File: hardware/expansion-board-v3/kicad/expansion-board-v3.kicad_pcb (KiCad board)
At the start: 6 copper layers, 100 x 62 mm, 178 parts, among them J1 J3_HAT_2x20_SMD排针, J2 U.FL_GNSS_EXT(经尾线转SMA), J4 USB-C_16P, J5 U.FL_978, J6 U.FL_1090_EXT(经尾线转SMA), J7 U.FL_IFA_TEST(π后调试口), J8 U.FL→内置patch, Q2 AO3401A, Q3 AO3401A, Q4 AO3401A, Q5 AO3401A, SW1 RESET短接焊盘, SW2 BOOTSEL短接焊盘, U1 ME6211C33M5, U10 CC1312R1F3RGZR, U11 QPL9547TR7, U12 BGA2817, U14 AD8313ARMZ, U15 TLV3501(TOKMAS), U16 XA17-G4K, U17 XA17-G4K, U2 TPS7A2033PDBVR, U3 TPS7A2033PDBVR, U4 BNO085, U5 BMP388, U6 QMC5883P, U7 ATGM336H-6N-74, U8 RP2040, U9 W25Q128JVSIQ, Y1 12MHz CL=10pF ABM8-272-T3, Y2 48MHz ABM8W-7pF, Y3 32.768kHz FC-135

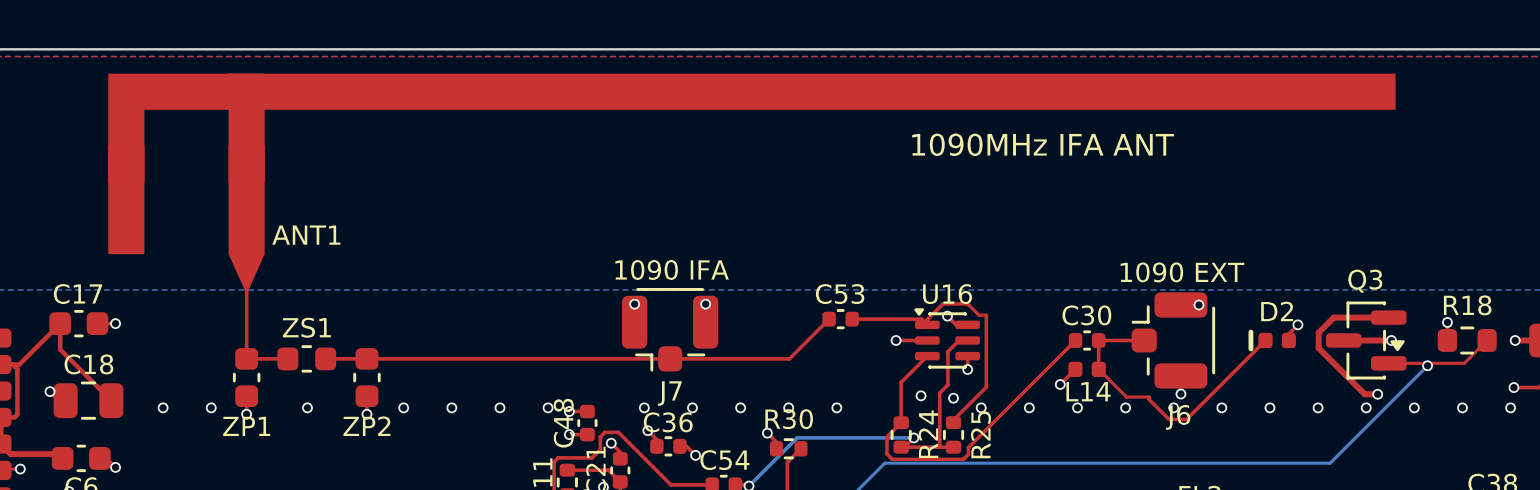
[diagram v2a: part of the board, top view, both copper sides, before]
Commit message: fix(pcb): 补上顶部禁铜带的 3.5mm 断口，换封装后强制重灌覆铜
天线开路端外侧本该全空，实际被 GND 铺铜灌了进去——倒 F 天线电场最强的
一头压着铜。**这正是旧版 IFA 被干扰的同一个病。**

## 根因：禁铜带是三块拼的，只有中间那块跟着天线走

    板级 ANT1090_short_end_keepout   板左沿 → ANT1 禁铜区左沿   坐标写死
    ANT1 封装自带的禁铜区             跟着天线几何走
    板级 ANT1090_open_end_keepout    ANT1 禁铜区右沿 → 板右沿   坐标写死

主臂由 53.5 缩到 50.0mm 后中间那块缩了 3.5mm，两边纹丝不动，带子上开了个
洞（v4 125.422..128.922 / v3 131.722..135.222）。gen_pcb.py 的注释里白纸
黑字写着"改天线位置要一起改"，但**写死的坐标不会提醒任何人**。

参考设计（4.3 原板）那条禁铜带是横跨整块板的矩形。所以判据不是"天线周围
留 2mm"，是**整条带从板左沿到板右沿连续**。

## 为什么整套自动检查都没抓到

    kicad-cli pcb drc --refill-zones   在内存里重填再检查 → 看到"填对的板子"
    kicad-cli pcb export gerbers       导出文件里存着的旧填充

「DRC 0 违例」和「Gerber 是错的」不矛盾，可以同时成立；而 gerber.sh 正是
这个顺序。焊盘落位检查只验"焊盘有没有对应 Flash"，铺铜多一块它不管。
缝里本来就没走线，DRC 更没话说。**只有看整块板才看得见。**

## 改动

- 两个 integrate_ifa_*.py：换 ANT1 后把两侧板级禁铜区贴合到 ANT1 禁铜区的
  **实测包围盒**，断言三块首尾相接铺满整板宽；Save 前 ZONE_FILLER 重灌
- gen_pcb.py：写死坐标改成从 ANT1 封装实测推导，否则整板重建洞会回来
- 新增 test_zone_fill_currency.py（5 项）：
  · 存盘覆铜必须是最新的（读板→记面积→内存重灌→比，通用，不针对天线）
  · 禁铜区内全铜层无铺铜（网格采样，点须严格落在区内）
  · 顶部禁铜带必须贯穿整板宽
  · 两条**坏样本自检**——现造"改了几何没重灌"和"带子断开"的板，
    验证上面的契约确实会红。写完就宣布有效是没有依据的
- test_v4_placement_contract：TP2–TP7 间距由 2.50 收到 2.033mm，
  跟随用户 2026-09-04 的手工重排（合同的既定口径是跟随实际板面）

## 验证

两版 kicad-cli pcb drc（**不加 --refill-zones**，验文件本身）0 违例 0 未连通；
顶部条带逐行与改动前对比完全一致，只剩射频馈线出口那一段；
投板 Gerber 6 层 19788 点采样落铜 0。

过程中我在同一处又犯了一次：用 KEEPOUT_LOCAL[3]（那是脚末端 y）当禁铜区
下沿，比多边形真实下沿少半个线宽，横向的洞刚补上又开了个纵向的。
**取实测边界，不要用公式重算。**
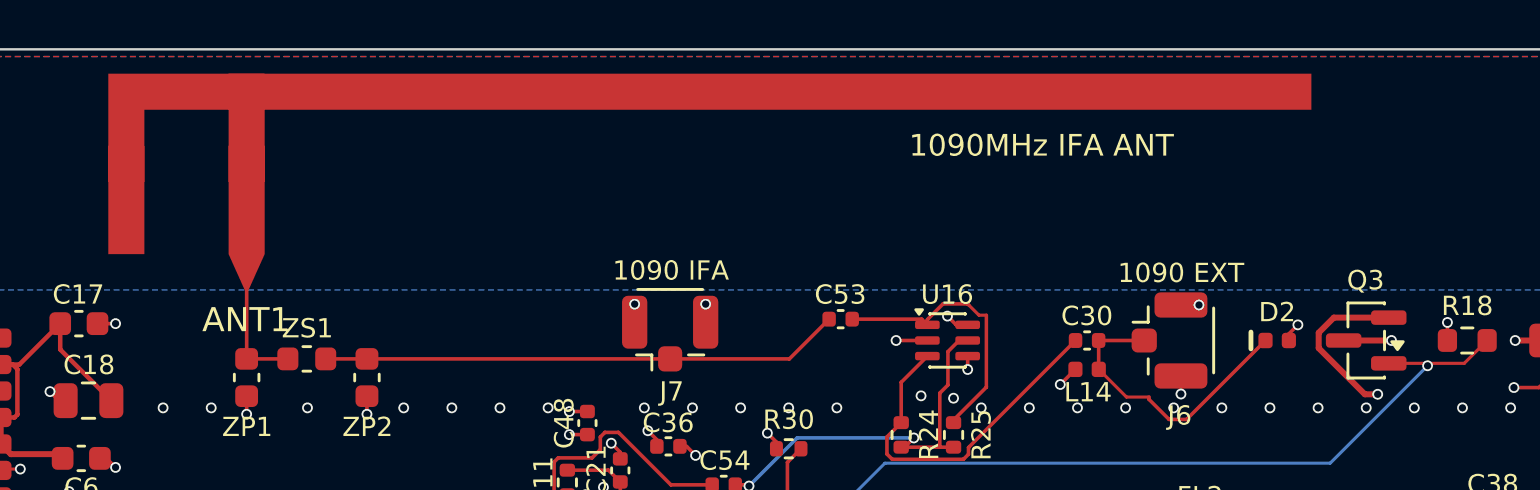
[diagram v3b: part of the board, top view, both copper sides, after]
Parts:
- ANT1: footprint expansion-board-v3:ANT_IFA_1090MHz -> ANT_IFA_1090MHz
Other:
- board text added: "V3.10 2026-09"
- board text removed: "V3.9 2026-09"
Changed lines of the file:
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@@
 		)
 	)
-	(footprint "expansion-board-v3:ANT_IFA_1090MHz"
-		(layer "F.Cu")
-		(at 85.46 57.75)
-		(descr "1090MHz 板载 IFA（完整六层rev2预研冻结画长）。主臂 52.0mm(名义切1.8mm至50.2mm；连续铜箔可按VNA继续切短) / 脚 6.0mm / 两脚中心距 4.988mm / 全段 1.5mm 等宽 / 四周净空 2.0mm。包络 53.5x7.5mm。脚全程在净空内，末端撞入 GND 铺铜。馈电腿铜箔外沿后含1.5mm长 1.5→0.15mm taper（几何rev2）。已 X 镜像使开路端远离 C6 2.4G 天线。")
-		(tags "antenna IFA 1090MHz ADS-B")
-		(property "Reference" "ANT1"
-			(at 2.54 0 0)
-			(layer "F.SilkS")
-			(effects
-				(font
-					(size 0.8 0.8)
-					(thickness 0.15)
-				)
-			)
-		)
-		(property "Value" "IFA_1090"
-			(at 0 5.2 0)
-			(layer "F.Fab")
-			(effects
-				(font
-					(size 1 1)
-					(thickness 0.15)
-				)
-			)
-		)
-		(property "Datasheet" ""
-			(at 0 0 0)
-			(layer "F.Fab")
-			(hide yes)
-			(effects
-				(font
-					(size 1.27 1.27)
-				)
-			)
-		)
-		(property "Description" ""
-			(at 0 0 0)
-			(layer "F.Fab")
-			(hide yes)
-			(effects
-				(font
-					(size 1.27 1.27)
-				)
-			)
-		)
-		(attr smd allow_missing_courtyard)
-		(net_tie_pad_groups "1, 2")
-		(duplicate_pad_numbers_are_jumpers no)
-		(fp_rect
-			(start -5.738 -6.738)
-			(end 47.762 0.762)
-			(stroke
-				(width 0.1)
-				(type default)
-			)
-			(fill no)
-			(layer "F.Fab")
-		)
-		(pad "1" smd custom
-			(at 0.012 -2.988)
-			(size 1.5 1.5)
-			(layers "F.Cu")
-			(net "ANT1090_IFA")
-			(options
-				(clearance outline)
-				(anchor rect)
-			)
-			(primitives
-				(gr_poly
-					(pts
-						(xy -0.75 3.75) (xy 0.75 3.75) (xy 0.75 -3.75) (xy -0.75 -3.75)
-					)
-					(width 0)
-					(fill yes)
-				)
-				(gr_poly
-					(pts
-						(xy -4.25 -3.75) (xy 47.75 -3.75) (xy 47.75 -2.25) (xy -4.25 -2.25)
-					)
-					(width 0)
-					(fill yes)
-				)
-				(gr_poly
-					(pts
-						(xy -0.75 3.75) (xy 0.75 3.75) (xy 0.075 5.25) (xy -0.075 5.25)
-					)
-					(width 0)
-					(fill yes)
-				)
-			)
-		)
-		(pad "2" smd custom
-			(at -4.988 -2.988)
-			(size 1.5 1.5)
-			(layers "F.Cu")
-			(net "GND")
-			(options
-				(clearance outline)
-				(anchor rect)
-			)
-			(primitives
-				(gr_poly
-					(pts
-						(xy -0.75 -3.75) (xy 0.75 -3.75) (xy 0.75 3.75) (xy -0.75 3.75)
-					)
-					(width 0)
-					(fill yes)
-				)
-			)
-		)
-		(zone
-			(layer "F.Cu")
-			(name "ifa_feed_channel")
-			(hatch edge 0.5)
-			(connect_pads
-				(clearance 0)
-			)
-			(min_thickness 0.25)
-			(keepout
-				(tracks allowed)
-				(vias allowed)
-				(pads allowed)
-				(copperpour not_allowed)
-				(footprints allowed)
-			)
-			(placement
-				(enabled no)
-				(sheetname "")
-			)
-			(fill
-				(thermal_gap 0.5)
-				(thermal_bridge_width 0.5)
-				(island_removal_mode 0)
-			)
-			(polygon
-				(pts
-					(xy 84.272 57.762) (xy 86.672 57.762) (xy 86.672 60.012) (xy 84.272 60.012)
-				)
-			)
-		)
-		(zone
-			(layers "F.Cu" "B.Cu" "In1.Cu" "In2.Cu" "In3.Cu" "In4.Cu")
-			(name "ifa_keepout")
-			(hatch edge 0.5)
-			(connect_pads
-				(clearance 0)
-			)
-			(min_thickness 0.25)
-			(keepout
-				(tracks not_allowed)
-				(vias not_allowed)
-				(pads allowed)
-				(copperpour not_allowed)
-				(footprints allowed)
-			)
-			(placement
-				(enabled no)
-				(sheetname "")
-			)
-			(fill
-				(thermal_gap 0.5)
-				(thermal_bridge_width 0.5)
-				(island_removal_mode 0)
-			)
-			(polygon
-				(pts
-					(xy 77.722 50.077) (xy 135.222 50.077) (xy 135.222 58.512) (xy 86.672 58.512) (xy 86.672 57.762)
-					(xy 84.272 57.762) (xy 84.272 58.512) (xy 77.722 58.512)
-				)
-			)
-		)
-		(embedded_fonts no)
-	)
 	(footprint "Connector_Coaxial:U.FL_Hirose_U.FL-R-SMT-1_Vertical"
 		(layer "F.Cu")
@@
 		)
 	)
+	(footprint "ANT_IFA_1090MHz"
+		(layer "F.Cu")
+		(at 85.46 57.75)
+		(descr "1090MHz 板载 IFA（V4.0实板装盒VNA定型）。主臂中心线 48.5mm / 脚 6.0mm / 两脚中心距 4.988mm / 全段 1.5mm 等宽 / 四周净空 2.0mm。包络 50.0x7.5mm。脚全程在净空内，末端撞入 GND 铺铜。馈电腿铜箔外沿后含1.5mm长 1.5→0.15mm taper（几何rev2）。已 X 镜像使开路端远离 C6 2.4G 天线。")
+		(tags "antenna IFA 1090MHz ADS-B")
+		(property "Reference" "ANT1"
+			(at 0 3.5 0)
+			(layer "F.SilkS")
+			(effects
+				(font
+					(size 1 1)
+					(thickness 0.15)
+				)
+			)
+		)
+		(property "Value" "IFA_1090"
+			(at 0 5.2 0)
+			(layer "F.Fab")
+			(effects
+				(font
+					(size 1 1)
+					(thickness 0.15)
+				)
+			)
+		)
+		(property "Datasheet" ""
+			(at 0 0 0)
+			(layer "F.Fab")
+			(hide yes)
+			(effects
+				(font
+					(size 1.27 1.27)
+				)
+			)
+		)
+		(property "Description" ""
+			(at 0 0 0)
+			(layer "F.Fab")
+			(hide yes)
+			(effects
+				(font
+					(size 1.27 1.27)
+				)
+			)
+		)
+		(attr smd allow_missing_courtyard)
+		(net_tie_pad_groups "1, 2")
+		(duplicate_pad_numbers_are_jumpers no)
+		(fp_rect
+			(start -5.738 -6.738)
+			(end 44.262 0.762)
+			(stroke
+				(width 0.1)
+				(type default)
+			)
+			(fill no)
+			(layer "F.Fab")
+		)
+		(pad "1" smd custom
+			(at 0.012 -2.988)
+			(size 1.5 1.5)
+			(layers "F.Cu")
+			(net "ANT1090_IFA")
+			(options
+				(clearance outline)
+				(anchor rect)
+			)
+			(primitives
+				(gr_poly
+					(pts
+						(xy -0.75 3.75) (xy 0.75 3.75) (xy 0.75 -3.75) (xy -0.75 -3.75)
+					)
+					(width 0)
+					(fill yes)
+				)
+				(gr_poly
+					(pts
+						(xy -4.25 -3.75) (xy 44.25 -3.75) (xy 44.25 -2.25) (xy -4.25 -2.25)
+					)
+					(width 0)
+					(fill yes)
+				)
+				(gr_poly
+					(pts
+						(xy -0.75 3.75) (xy 0.75 3.75) (xy 0.075 5.25) (xy -0.075 5.25)
+					)
+					(width 0)
+					(fill yes)
+				)
+			)
+		)
+		(pad "2" smd custom
+			(at -4.988 -2.988)
+			(size 1.5 1.5)
+			(layers "F.Cu")
+			(net "GND")
+			(options
+				(clearance outline)
+				(anchor rect)
+			)
+			(primitives
+				(gr_poly
+					(pts
+						(xy -0.75 -3.75) (xy 0.75 -3.75) (xy 0.75 3.75) (xy -0.75 3.75)
+					)
+					(width 0)
+					(fill yes)
+				)
+			)
+		)
+		(zone
+			(layer "F.Cu")
+			(name "ifa_feed_channel")
+			(hatch edge 0.5)
+			(connect_pads
+				(clearance 0)
+			)
+			(min_thickness 0.25)
+			(keepout
+				(tracks allowed)
+				(vias allowed)
+				(pads allowed)
+				(copperpour not_allowed)
+				(footprints allowed)
+			)
+			(placement
+				(enabled no)
+				(sheetname "")
+			)
+			(fill
+				(thermal_gap 0.5)
+				(thermal_bridge_width 0.5)
+				(island_removal_mode 0)
+			)
+			(polygon
+				(pts
+					(xy 84.272 57.762) (xy 86.672 57.762) (xy 86.672 60.012) (xy 84.272 60.012)
+				)
+			)
+		)
+		(zone
+			(layers "F.Cu" "B.Cu" "In1.Cu" "In2.Cu" "In3.Cu" "In4.Cu")
+			(name "ifa_keepout")
+			(hatch edge 0.5)
+			(connect_pads
+				(clearance 0)
+			)
+			(min_thickness 0.25)
+			(keepout
+				(tracks not_allowed)
+				(vias not_allowed)
+				(pads allowed)
+				(copperpour not_allowed)
+				(footprints allowed)
+			)
+			(placement
+				(enabled no)
+				(sheetname "")
+			)
+			(fill
+				(thermal_gap 0.5)
+				(thermal_bridge_width 0.5)
+				(island_removal_mode 0)
+			)
+			(polygon
+				(pts
+					(xy 77.722 50.077) (xy 131.722 50.077) (xy 131.722 58.512) (xy 86.672 58.512) (xy 86.672 57.762)
+					(xy 84.272 57.762) (xy 84.272 58.512) (xy 77.722 58.512)
+				)
+			)
+		)
+		(embedded_fonts no)
+	)
 	(footprint "Capacitor_SMD:C_0603_1608Metric"
 		(layer "F.Cu")
@@
 		)
 	)
-	(gr_text "V3.9   2026-09"
+	(gr_text "V3.10   2026-09"
 		(at 100 80 0)
 		(layer "B.SilkS")
@@
 	)
 	(segment
-		(start 85.472 60.012)
-		(end 85.472 62.865)
-		(width 0.15)
-		(layer "F.Cu")
-		(net "ANT1090_IFA")
-	)
-	(segment
-		(start 85.472 62.865)
-		(end 87.1845 62.865)
-		(width 0.15)
-		(layer "F.Cu")
-		(net "ANT1090_IFA")
-	)
-	(segment
 		(start 108.028 62.865)
 		(end 109.679 61.214)
@@
 	)
 	(segment
+		(start 85.472 60.012)
+		(end 85.472 62.865)
+		(width 0.15)
+		(layer "F.Cu")
+		(net "ANT1090_IFA")
+	)
+	(segment
+		(start 85.472 62.865)
+		(end 87.1845 62.865)
+		(width 0.15)
+		(layer "F.Cu")
+		(net "ANT1090_IFA")
+	)
+	(segment
 		(start 133.0505 62.1)
 		(end 131.0625 62.1)
@@
 		(polygon
 			(pts
-				(xy 135.222 50.077) (xy 150 50.077) (xy 150 58.512) (xy 135.222 58.512)
+				(xy 131.722 50.077) (xy 150 50.077) (xy 150 58.512) (xy 131.722 58.512)
 			)
 		)

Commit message: hardware: v4 走线固化 + V4.5 发布包 + 装配站点/子项目
- v3/v4 kicad_pcb 重新布线; export_routes 快照 ROUTES.json(1609 段/438 孔)。
- V4.5 Gerber/KiCad 发布包(20260911); cal-board/fpc-antenna 子项目;
  web/assembly 装配站点与生成工具; V4.6 airband BOM 草案。
- 文档: BASEBOARD_REF / ASSEMBLY / SELECTIVE_PLACEMENT 等同步。
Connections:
- Q4 pad 2: 3V3_GNSS -> GNSS_VCC_RF
- Q5 pad 2: 3V3_GNSS -> GNSS_VCC_RF
- U7 pad 14: unconnected-(U7-VCC_RF-Pad14) -> GNSS_VCC_RF
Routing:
- net 3V3_GNSS: track 172.3 -> 156.3 mm
- net GNSS_VCC_RF: track 0.00 -> 14.5 mm
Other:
- board text added: "V3.11 2026-09"
- board text removed: "V3.10 2026-09"
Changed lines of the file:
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@@
 			(layers "F.Cu" "F.Mask" "F.Paste")
 			(roundrect_rratio 0.25)
-			(net "unconnected-(U7-VCC_RF-Pad14)")
+			(net "GNSS_VCC_RF")
 		)
 		(pad "15" smd roundrect
@@
 			(layers "F.Cu" "F.Mask" "F.Paste")
 			(roundrect_rratio 0.25)
-			(net "3V3_GNSS")
+			(net "GNSS_VCC_RF")
 		)
 		(pad "3" smd roundrect
@@
 			(layers "F.Cu" "F.Mask" "F.Paste")
 			(roundrect_rratio 0.25)
-			(net "3V3_GNSS")
+			(net "GNSS_VCC_RF")
 		)
 		(pad "3" smd roundrect
@@
 		)
 	)
-	(gr_text "V3.10   2026-09"
+	(gr_text "V3.11   2026-09"
 		(at 100 80 0)
 		(layer "B.SilkS")
@@
 	)
 	(segment
-		(start 60.8625 71.15)
-		(end 61.203 71.4905)
-		(width 0.25)
-		(layer "F.Cu")
-		(net "3V3_GNSS")
-	)
-	(segment
-		(start 56.8625 73.55)
-		(end 59.2113 73.55)
-		(width 0.25)
-		(layer "F.Cu")
-		(net "3V3_GNSS")
-	)
-	(segment
-		(start 60.8625 71.8988)
-		(end 60.8625 71.15)
-		(width 0.25)
-		(layer "F.Cu")
-		(net "3V3_GNSS")
-	)
-	(segment
-		(start 61.203 71.4905)
-		(end 69.4219 71.4905)
-		(width 0.25)
-		(layer "F.Cu")
-		(net "3V3_GNSS")
-	)
-	(segment
 		(start 124.1625 105.4325)
 		(end 124.1625 106.15)
@@
 	)
 	(segment
-		(start 59.2113 73.55)
-		(end 60.8625 71.8988)
-		(width 0.25)
-		(layer "F.Cu")
-		(net "3V3_GNSS")
-	)
-	(segment
 		(start 73.6176 94.25)
 		(end 73.1625 94.25)
@@
 	)
 	(segment
-		(start 69.4219 71.4905)
-		(end 70.7154 70.197)
-		(width 0.25)
-		(layer "F.Cu")
-		(net "3V3_GNSS")
-	)
-	(segment
 		(start 130.6536 61.15)
 		(end 130.0256 61.778)
@@
 	)
 	(segment
+		(start 85.472 60.012)
+		(end 85.472 62.865)
+		(width 0.15)
+		(layer "F.Cu")
+		(net "ANT1090_IFA")
+	)
+	(segment
+		(start 85.472 62.865)
+		(end 87.1845 62.865)
+		(width 0.15)
+		(layer "F.Cu")
+		(net "ANT1090_IFA")
+	)
+	(segment
 		(start 115.825 87.3)
 		(end 118.375 87.3)
@@
 	)
 	(segment
+		(start 60.125 71.35)
+		(end 60.8625 71.15)
+		(width 0.15)
+		(layer "F.Cu")
+		(net "GNSS_VCC_RF")
+	)
+	(segment
+		(start 63.7 70.9)
+		(end 64.599999 70)
+		(width 0.15)
+		(layer "F.Cu")
+		(net "GNSS_VCC_RF")
+	)
+	(segment
+		(start 60.1 72.85)
+		(end 60.1 71.35)
+		(width 0.15)
+		(layer "F.Cu")
+		(net "GNSS_VCC_RF")
+	)
+	(segment
+		(start 61.6 70.9)
+		(end 60.8625 71.15)
+		(width 0.15)
+		(layer "F.Cu")
+		(net "GNSS_VCC_RF")
+	)
+	(segment
+		(start 64.65 66.4)
+		(end 64.599999 66.4)
+		(width 0.15)
+		(layer "F.Cu")
+		(net "GNSS_VCC_RF")
+	)
+	(segment
+		(start 57.55 73.3)
+		(end 59.65 73.3)
+		(width 0.15)
+		(layer "F.Cu")
+		(net "GNSS_VCC_RF")
+	)
+	(segment
+		(start 61.6 70.9)
+		(end 63.7 70.9)
+		(width 0.15)
+		(layer "F.Cu")
+		(net "GNSS_VCC_RF")
+	)
+	(segment
+		(start 65.55 66.4)
+		(end 64.65 66.4)
+		(width 0.15)
+		(layer "F.Cu")
+		(net "GNSS_VCC_RF")
+	)
+	(segment
+		(start 60.125 71.35)
+		(end 60.1 71.35)
+		(width 0.15)
+		(layer "F.Cu")
+		(net "GNSS_VCC_RF")
+	)
+	(segment
+		(start 57.55 73.3)
+		(end 56.8625 73.55)
+		(width 0.15)
+		(layer "F.Cu")
+		(net "GNSS_VCC_RF")
+	)
+	(segment
+		(start 64.599999 70)
+		(end 64.599999 66.4)
+		(width 0.15)
+		(layer "F.Cu")
+		(net "GNSS_VCC_RF")
+	)
+	(segment
+		(start 59.65 73.3)
+		(end 60.1 72.85)
+		(width 0.15)
+		(layer "F.Cu")
+		(net "GNSS_VCC_RF")
+	)
+	(segment
 		(start 106.48 71.2)
 		(end 108.8 71.2)
@@
 	)
 	(segment
-		(start 85.472 60.012)
-		(end 85.472 62.865)
-		(width 0.15)
-		(layer "F.Cu")
-		(net "ANT1090_IFA")
-	)
-	(segment
-		(start 85.472 62.865)
-		(end 87.1845 62.865)
-		(width 0.15)
-		(layer "F.Cu")
-		(net "ANT1090_IFA")
-	)
-	(segment
